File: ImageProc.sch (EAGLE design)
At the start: 113 parts, among them IC1 XC61GC3002HR-G, IC2 MIC5335-SPYMT, IC3 MIC5335-JGYMT, IC5 AT86RF233-ZU, IC6 LTC6088, IC7 DRV8833RTY, IC8 DRV8833RTY, IC9 MPU-6000, P1 BAT+, P10 MD2, P11 EXT1, P12 EXT2, P13 EXT3, P14 EXT4, P16 EXT5, P2 BAT-, P3 MA1, P4 MA2, P5 MB1, P6 MB2, P7 MC1, P8 MC2, P9 MD1, U1 CY8C5688LTI-LP086, U2 USD-SOCKETNEW

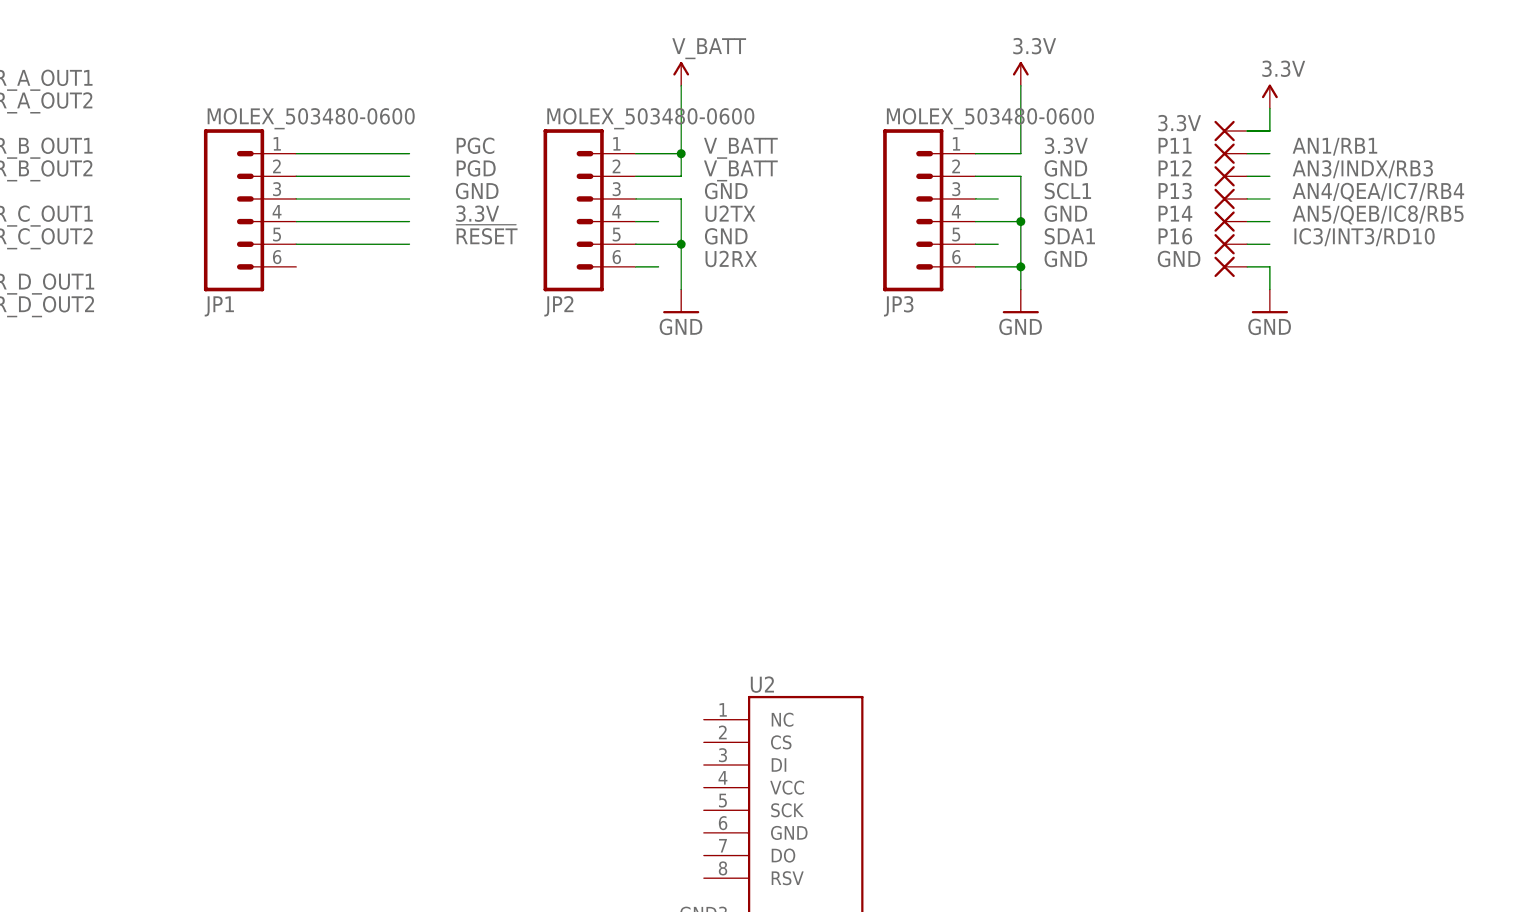
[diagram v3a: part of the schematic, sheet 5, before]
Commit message: Still removing small elemets from existing IP2.5
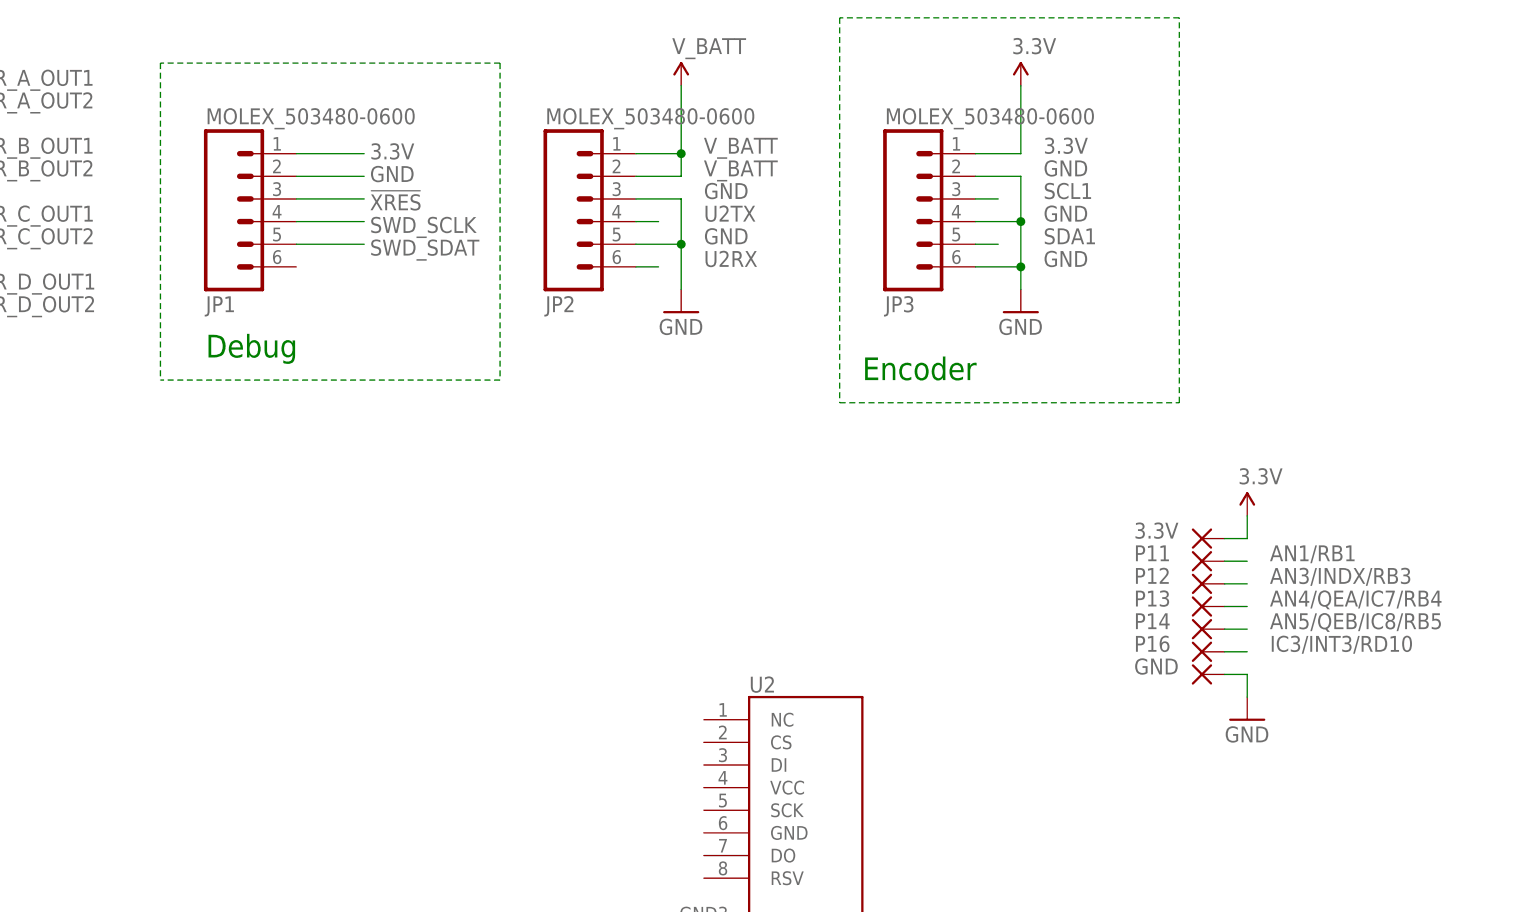
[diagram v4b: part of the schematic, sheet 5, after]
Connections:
- removed net !RESET: IC5S.!RST, JP1.5, R3.1
- removed net PGC: JP1.1
- removed net PGD: JP1.2
- new net !XRES: IC5S.!RST, JP1.3, R3.1
- new net SWD_SCLK: JP1.4
- new net SWD_SDAT: JP1.5
- net 3.3V: now also JP1.1; no longer JP1.4
- net GND: now also JP1.2; no longer JP1.3
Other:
- note added: "Debug"
- note added: "Encoder"
- moved on the sheet: 3.3V, GND, P11, P12, P13, P14, P16
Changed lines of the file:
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@@
 <setting verticaltext="up"/>
 </settings>
-<grid distance="0.1" unitdist="inch" unit="inch" style="lines" multiple="1" display="no" altdistance="0.01" altunitdist="inch" altunit="inch"/>
+<grid distance="0.1" unitdist="inch" unit="inch" style="lines" multiple="1" display="no" altdistance="0.025" altunitdist="inch" altunit="inch"/>
 <layers>
 <layer number="1" name="Top" color="4" fill="1" visible="no" active="no"/>
@@
 </segment>
 </net>
-<net name="!RESET" class="0">
+<net name="!XRES" class="0">
 <segment>
 <pinref part="R3" gate="G$1" pin="1"/>
@@
 </segment>
 </net>
-<net name="!RESET" class="0">
+<net name="!XRES" class="0">
 <segment>
 <label x="66.04" y="119.38" size="1.778" layer="95"/>
@@
 <description>Connectors and Peripherals</description>
 <plain>
+<text x="172.72" y="134.62" size="2.54" layer="91">Encoder</text>
+<text x="99.06" y="137.16" size="2.54" layer="91">Debug</text>
 </plain>
 <instances>
@@
 <attribute name="NAME" x="45.72" y="38.1" size="1.778" layer="95"/>
 </instance>
-<instance part="P11" gate="1" x="213.36" y="160.02" smashed="yes">
-<attribute name="NAME" x="205.74" y="160.02" size="1.778" layer="95"/>
-</instance>
-<instance part="P12" gate="1" x="213.36" y="157.48" smashed="yes">
-<attribute name="NAME" x="205.74" y="157.48" size="1.778" layer="95"/>
-</instance>
-<instance part="P13" gate="1" x="213.36" y="154.94" smashed="yes">
-<attribute name="NAME" x="205.74" y="154.94" size="1.778" layer="95"/>
-</instance>
-<instance part="P14" gate="1" x="213.36" y="152.4" smashed="yes">
-<attribute name="NAME" x="205.74" y="152.4" size="1.778" layer="95"/>
-</instance>
-<instance part="P16" gate="1" x="213.36" y="149.86" smashed="yes">
-<attribute name="NAME" x="205.74" y="149.86" size="1.778" layer="95"/>
-</instance>
-<instance part="GND" gate="1" x="213.36" y="147.32" smashed="yes">
-<attribute name="NAME" x="205.74" y="147.32" size="1.778" layer="95"/>
-</instance>
-<instance part="3.3V" gate="1" x="213.36" y="162.56" smashed="yes">
-<attribute name="NAME" x="205.74" y="162.56" size="1.778" layer="95"/>
-</instance>
-<instance part="P+1" gate="G$1" x="218.44" y="165.1"/>
-<instance part="GND24" gate="1" x="218.44" y="142.24"/>
+<instance part="P11" gate="1" x="210.82" y="114.3" smashed="yes">
+<attribute name="NAME" x="203.2" y="114.3" size="1.778" layer="95"/>
+</instance>
+<instance part="P12" gate="1" x="210.82" y="111.76" smashed="yes">
+<attribute name="NAME" x="203.2" y="111.76" size="1.778" layer="95"/>
+</instance>
+<instance part="P13" gate="1" x="210.82" y="109.22" smashed="yes">
+<attribute name="NAME" x="203.2" y="109.22" size="1.778" layer="95"/>
+</instance>
+<instance part="P14" gate="1" x="210.82" y="106.68" smashed="yes">
+<attribute name="NAME" x="203.2" y="106.68" size="1.778" layer="95"/>
+</instance>
+<instance part="P16" gate="1" x="210.82" y="104.14" smashed="yes">
+<attribute name="NAME" x="203.2" y="104.14" size="1.778" layer="95"/>
+</instance>
+<instance part="GND" gate="1" x="210.82" y="101.6" smashed="yes">
+<attribute name="NAME" x="203.2" y="101.6" size="1.778" layer="95"/>
+</instance>
+<instance part="3.3V" gate="1" x="210.82" y="116.84" smashed="yes">
+<attribute name="NAME" x="203.2" y="116.84" size="1.778" layer="95"/>
+</instance>
+<instance part="P+1" gate="G$1" x="215.9" y="119.38"/>
+<instance part="GND24" gate="1" x="215.9" y="96.52"/>
 <instance part="U2" gate="G$1" x="162.56" y="83.82"/>
 </instances>
@@
 <pinref part="GND" gate="1" pin="P"/>
 <pinref part="GND24" gate="1" pin="GND"/>
-<wire x1="215.9" y1="147.32" x2="218.44" y2="147.32" width="0.1524" layer="91"/>
-<wire x1="218.44" y1="147.32" x2="218.44" y2="144.78" width="0.1524" layer="91"/>
-</segment>
-<segment>
-<pinref part="JP1" gate="G$1" pin="3"/>
-<wire x1="109.22" y1="154.94" x2="121.92" y2="154.94" width="0.1524" layer="91"/>
-<label x="127" y="154.94" size="1.778" layer="95"/>
+<wire x1="213.36" y1="101.6" x2="215.9" y2="101.6" width="0.1524" layer="91"/>
+<wire x1="215.9" y1="101.6" x2="215.9" y2="99.06" width="0.1524" layer="91"/>
+</segment>
+<segment>
+<pinref part="JP1" gate="G$1" pin="2"/>
+<wire x1="109.22" y1="157.48" x2="116.84" y2="157.48" width="0.1524" layer="91"/>
+<label x="117.475" y="156.845" size="1.778" layer="95"/>
 </segment>
 </net>
@@
 <wire x1="25.4" y1="109.22" x2="20.32" y2="109.22" width="0.1524" layer="91"/>
 <label x="10.16" y="109.22" size="1.778" layer="95"/>
-</segment>
-</net>
-<net name="!RESET" class="0">
-<segment>
-<pinref part="JP1" gate="G$1" pin="5"/>
-<wire x1="109.22" y1="149.86" x2="121.92" y2="149.86" width="0.1524" layer="91"/>
-<label x="127" y="149.86" size="1.778" layer="95"/>
 </segment>
 </net>
@@
 <segment>
 <pinref part="3.3V" gate="1" pin="P"/>
-<wire x1="215.9" y1="162.56" x2="218.44" y2="162.56" width="0.1524" layer="91"/>
 <pinref part="P+1" gate="G$1" pin="3.3V"/>
-<wire x1="218.44" y1="162.56" x2="218.44" y2="165.1" width="0.1524" layer="91"/>
-<wire x1="215.9" y1="162.56" x2="218.44" y2="162.56" width="0.1524" layer="91"/>
-</segment>
-<segment>
-<pinref part="JP1" gate="G$1" pin="4"/>
-<wire x1="109.22" y1="152.4" x2="121.92" y2="152.4" width="0.1524" layer="91"/>
-<label x="127" y="152.4" size="1.778" layer="95"/>
+<wire x1="215.9" y1="116.84" x2="215.9" y2="119.38" width="0.1524" layer="91"/>
+<wire x1="213.36" y1="116.84" x2="215.9" y2="116.84" width="0.1524" layer="91"/>
+</segment>
+<segment>
+<pinref part="JP1" gate="G$1" pin="1"/>
+<wire x1="109.22" y1="160.02" x2="116.84" y2="160.02" width="0.1524" layer="91"/>
+<label x="117.475" y="159.385" size="1.778" layer="95"/>
 </segment>
 </net>
@@
 <segment>
 <pinref part="P11" gate="1" pin="P"/>
-<wire x1="215.9" y1="160.02" x2="218.44" y2="160.02" width="0.1524" layer="91"/>
-<label x="220.98" y="160.02" size="1.778" layer="95"/>
+<wire x1="213.36" y1="114.3" x2="215.9" y2="114.3" width="0.1524" layer="91"/>
+<label x="218.44" y="114.3" size="1.778" layer="95"/>
 </segment>
 </net>
@@
 <segment>
 <pinref part="P12" gate="1" pin="P"/>
-<wire x1="215.9" y1="157.48" x2="218.44" y2="157.48" width="0.1524" layer="91"/>
-<label x="220.98" y="157.48" size="1.778" layer="95"/>
+<wire x1="213.36" y1="111.76" x2="215.9" y2="111.76" width="0.1524" layer="91"/>
+<label x="218.44" y="111.76" size="1.778" layer="95"/>
 </segment>
 </net>
@@
 <segment>
 <pinref part="P13" gate="1" pin="P"/>
-<wire x1="215.9" y1="154.94" x2="218.44" y2="154.94" width="0.1524" layer="91"/>
-<label x="220.98" y="154.94" size="1.778" layer="95"/>
+<wire x1="213.36" y1="109.22" x2="215.9" y2="109.22" width="0.1524" layer="91"/>
+<label x="218.44" y="109.22" size="1.778" layer="95"/>
 </segment>
 </net>
@@
 <segment>
 <pinref part="P14" gate="1" pin="P"/>
-<wire x1="215.9" y1="152.4" x2="218.44" y2="152.4" width="0.1524" layer="91"/>
-<label x="220.98" y="152.4" size="1.778" layer="95"/>
+<wire x1="213.36" y1="106.68" x2="215.9" y2="106.68" width="0.1524" layer="91"/>
+<label x="218.44" y="106.68" size="1.778" layer="95"/>
 </segment>
 </net>
@@
 <segment>
 <pinref part="P16" gate="1" pin="P"/>
-<wire x1="215.9" y1="149.86" x2="218.44" y2="149.86" width="0.1524" layer="91"/>
-<label x="220.98" y="149.86" size="1.778" layer="95"/>
-</segment>
-</net>
-<net name="PGC" class="0">
-<segment>
-<pinref part="JP1" gate="G$1" pin="1"/>
-<wire x1="109.22" y1="160.02" x2="121.92" y2="160.02" width="0.1524" layer="91"/>
-<label x="127" y="160.02" size="1.778" layer="95"/>
-</segment>
-</net>
-<net name="PGD" class="0">
-<segment>
-<pinref part="JP1" gate="G$1" pin="2"/>
-<wire x1="109.22" y1="157.48" x2="121.92" y2="157.48" width="0.1524" layer="91"/>
-<label x="127" y="157.48" size="1.778" layer="95"/>
-</segment>
-</net>
+<wire x1="213.36" y1="104.14" x2="215.9" y2="104.14" width="0.1524" layer="91"/>
+<label x="218.44" y="104.14" size="1.778" layer="95"/>
+</segment>
+</net>
+<net name="N$33" class="0">
+<segment>
+<wire x1="170.18" y1="175.26" x2="170.18" y2="132.08" width="0.1524" layer="91" style="shortdash"/>
+<wire x1="170.18" y1="132.08" x2="208.28" y2="132.08" width="0.1524" layer="91" style="shortdash"/>
+<wire x1="208.28" y1="132.08" x2="208.28" y2="175.26" width="0.1524" layer="91" style="shortdash"/>
+<wire x1="208.28" y1="175.26" x2="170.18" y2="175.26" width="0.1524" layer="91" style="shortdash"/>
+</segment>
+<segment>
+<wire x1="93.98" y1="170.18" x2="93.98" y2="134.62" width="0.1524" layer="91" style="shortdash"/>
+</segment>
+<segment>
+<wire x1="132.08" y1="170.18" x2="93.98" y2="170.18" width="0.1524" layer="91" style="shortdash"/>
+</segment>
+<segment>
+<wire x1="132.08" y1="134.62" x2="93.98" y2="134.62" width="0.1524" layer="91" style="shortdash"/>
+</segment>
+<segment>
+<wire x1="132.08" y1="170.18" x2="132.08" y2="134.62" width="0.1524" layer="91" style="shortdash"/>
+</segment>
+</net>
+<net name="!XRES" class="0">
+<segment>
+<pinref part="JP1" gate="G$1" pin="3"/>
+<wire x1="109.22" y1="154.94" x2="116.84" y2="154.94" width="0.1524" layer="91"/>
+<label x="117.475" y="153.67" size="1.778" layer="95"/>
+</segment>
+</net>
+<net name="SWD_SCLK" class="0">
+<segment>
+<pinref part="JP1" gate="G$1" pin="4"/>
+<wire x1="109.22" y1="152.4" x2="116.84" y2="152.4" width="0.1524" layer="91"/>
+<label x="117.475" y="151.13" size="1.778" layer="95"/>
+</segment>
+</net>
+<net name="SWD_SDAT" class="0">
+<segment>
+<pinref part="JP1" gate="G$1" pin="5"/>
+<wire x1="109.22" y1="149.86" x2="116.84" y2="149.86" width="0.1524" layer="91"/>
+<label x="117.475" y="148.59" size="1.778" layer="95"/>
+</segment>
+</net>

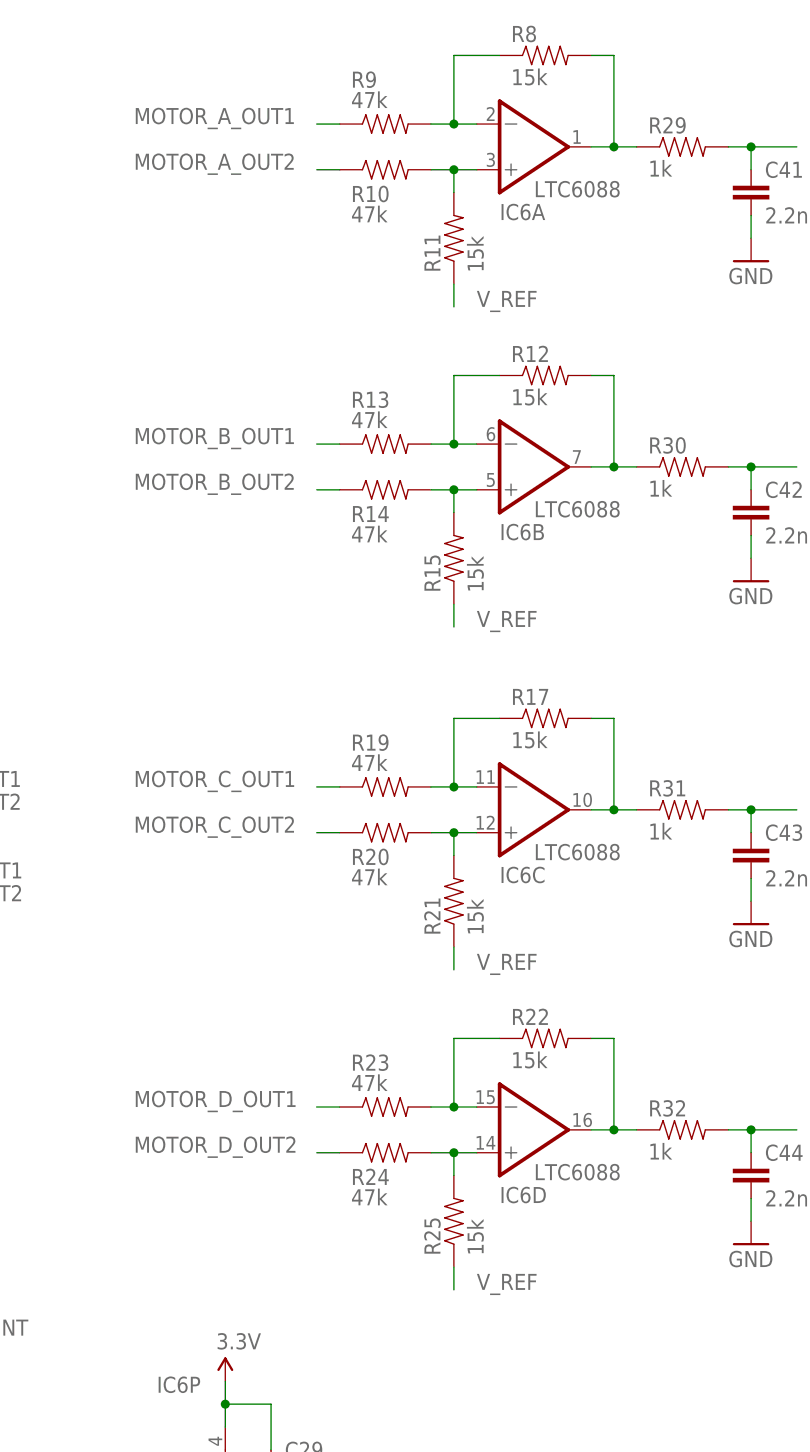
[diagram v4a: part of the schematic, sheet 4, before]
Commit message: Changed to resistor arrays. SD card footprint updated. Much routing removed.
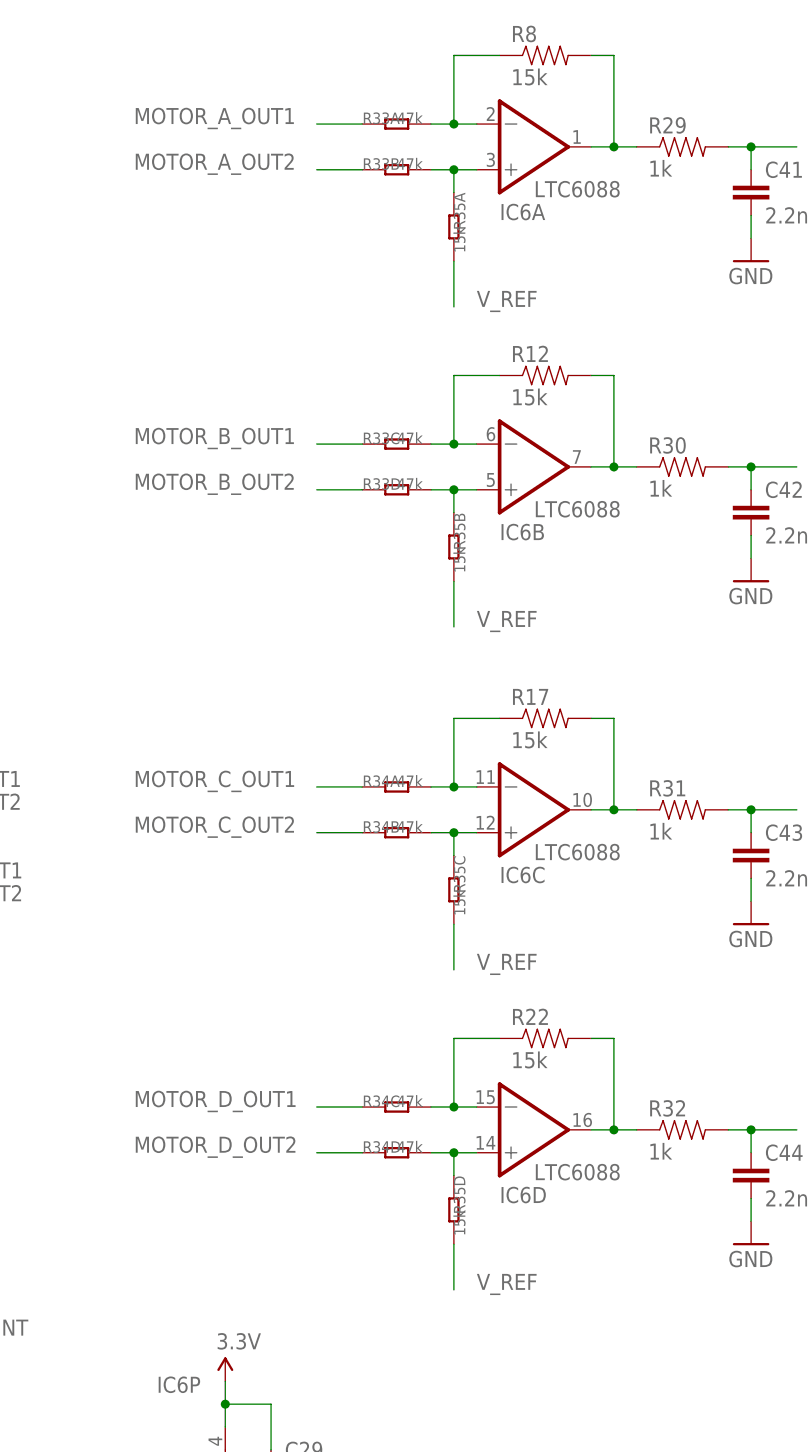
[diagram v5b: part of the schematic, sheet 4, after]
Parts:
- removed 3.3V, GND, P16: EXT5, wirepad:SMD2
- removed C2, C5, C8: 1uF, biomimetic:CAP0402-CAP
- removed IC3: MIC5335-JGYMT, biomimetic:MIC5335-JGYMT
- removed P11: EXT1, wirepad:SMD2
- removed P12: EXT2, wirepad:SMD2
- removed P13: EXT3, wirepad:SMD2
- removed P14: EXT4, wirepad:SMD2
- removed R10, R13, R14, R19, R20, R23, R24, R9: 47k, biomimetic:RESISTOR0402-RES
- removed R11, R15, R21, R25: 15k, biomimetic:RESISTOR0402-RES
- removed U2: USD-SOCKETNEW, SparkFun-Connectors:USD-SOCKETNEW
- added J1: CON-HRS-DM3AT, pullin:CON-HRS-DM3AT
- added R33, R34: 47k, OPL Eagle Library:R-4R
- added R35: 15k, OPL Eagle Library:R-4R
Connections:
- removed net 1.8V: C8.1, IC3.1.8V
- removed net 2.5V: C2.1, IC3.2.5V
- removed net AN1/RB1: P11.P
- removed net AN3/INDX/RB3: P12.P
- removed net AN4/QEA/IC7/RB4: P13.P
- removed net AN5/QEB/IC8/RB5: P14.P
- removed net IC3/INT3/RD10: P16.P
- net 3.3V: no longer 3.3V.P
- net GND: no longer C2.2, C5.1, C8.2, GND.P, IC3.GND
- net MOTOR_A_OUT1: no longer R9.1
- net MOTOR_A_OUT2: no longer R10.1
- net MOTOR_B_OUT1: no longer R13.1
- net MOTOR_B_OUT2: no longer R14.1
- net MOTOR_C_OUT1: no longer R19.1
- net MOTOR_C_OUT2: no longer R20.1
- net MOTOR_D_OUT1: no longer R23.1
- net MOTOR_D_OUT2: no longer R24.1
- net N$22: now also R33C.2; no longer R13.2
- net N$23: now also R33D.2, R35B.1; no longer R14.2, R15.2
- net N$24: now also R34A.2; no longer R19.2
- net N$25: now also R34B.2, R35C.1; no longer R20.2, R21.2
- net N$26: now also R34C.2; no longer R23.2
- net N$27: now also R34D.2, R35D.1; no longer R24.2, R25.2
- net N$30: now also R33A.2; no longer R9.2
- net N$31: now also R33B.2, R35A.1; no longer R10.2, R11.2
- net V_BATT: no longer C5.2, IC3.EN_1.8V, IC3.EN_2.5V, IC3.VIN
- net V_REF: no longer R11.1, R15.1, R21.1, R25.1
